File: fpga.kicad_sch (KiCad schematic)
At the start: 53 parts, among them Q1 BSS138PW, Q2 BSS138PW, Q3 BSS138PW, Q4 BSS138PW, SW1 SW_B3U-1000P_SMD, U1 ICE40UP5K-SG48, U2 FT232H_QFN, U3 W25Q32JW_SOIC-8

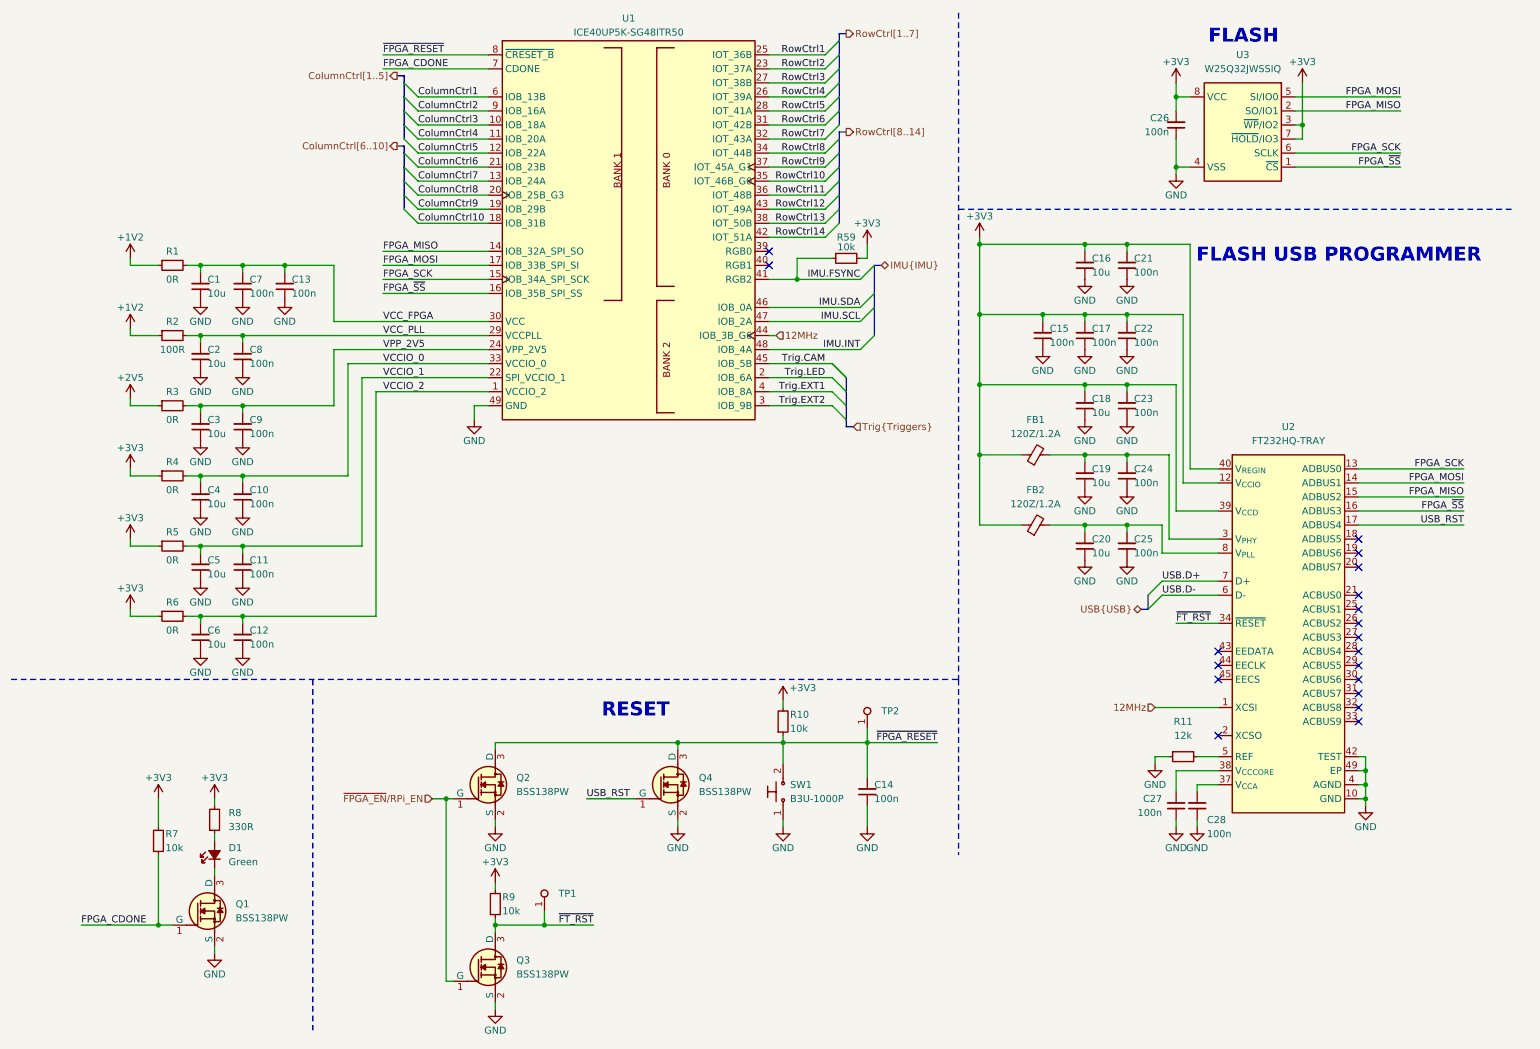
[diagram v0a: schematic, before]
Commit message: [#72133] Sch: Update control hierarchy
Signed-off-by: Dawid Lentka <dlentka@antmicro.com>
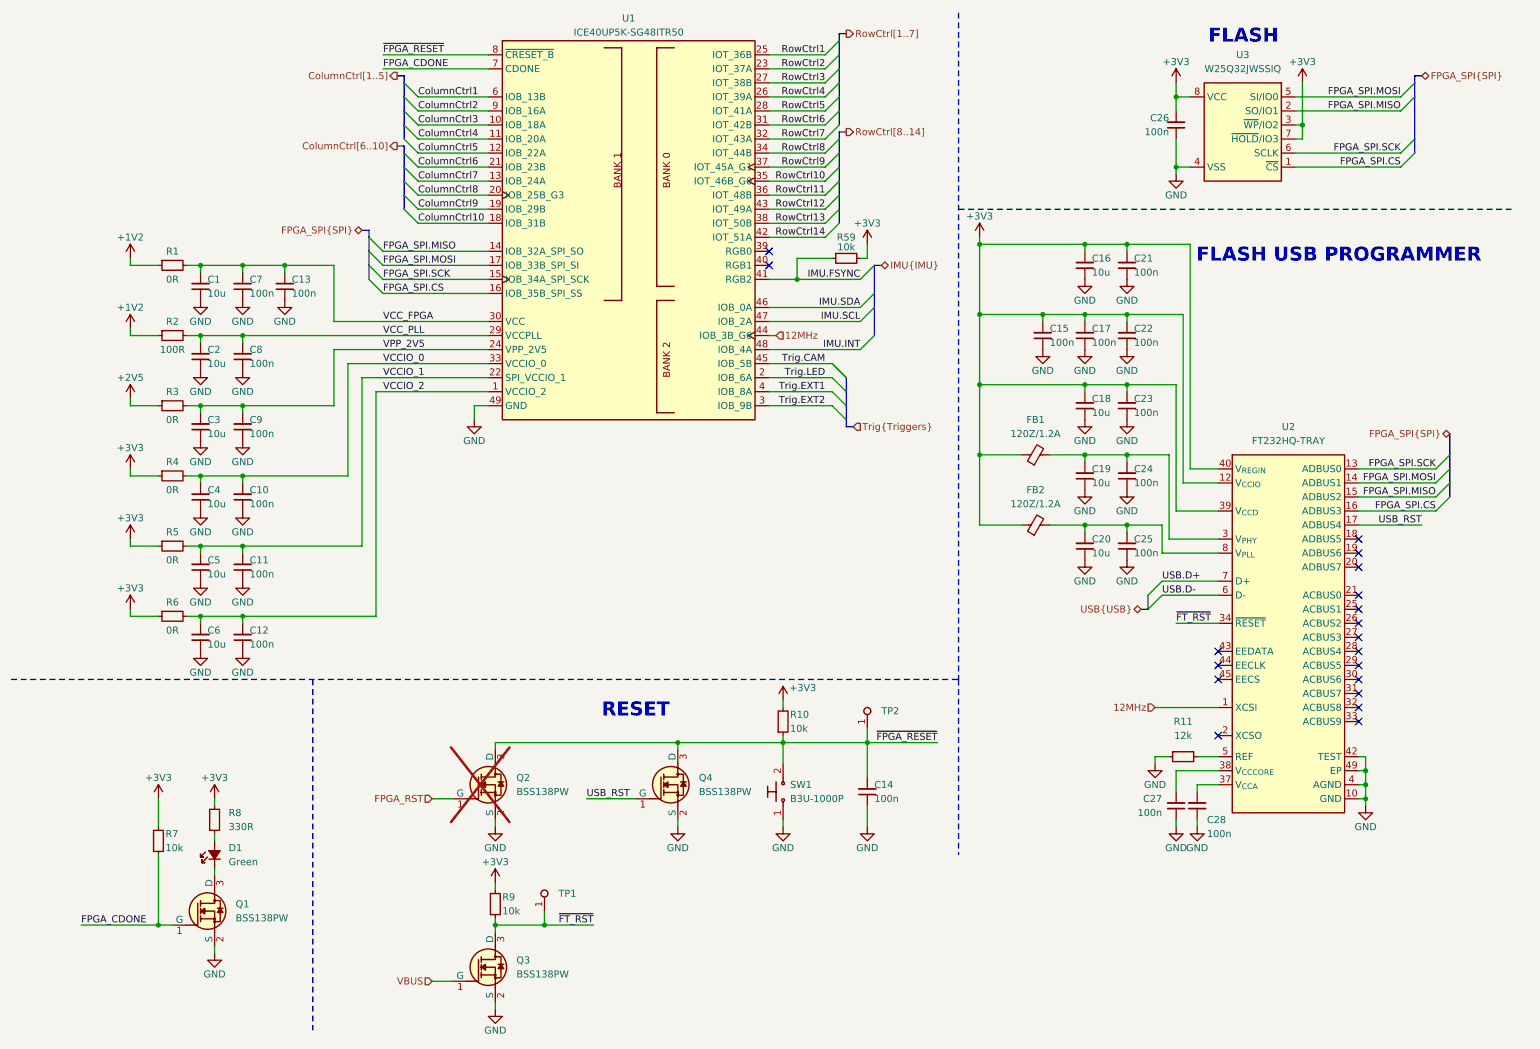
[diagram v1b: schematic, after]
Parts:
- Q2: now not fitted
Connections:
- net FPGA_MISO renamed FPGA_SPI.MISO
- net FPGA_MOSI renamed FPGA_SPI.MOSI
- net FPGA_SCK renamed FPGA_SPI.SCK
- net FPGA_~{SS} renamed FPGA_SPI.CS
- net ~{FPGA_EN}/RPi_EN renamed FPGA_RST
- net FPGA_RST: no longer Q3.1 (G)
- new net VBUS: Q3.1 (G)

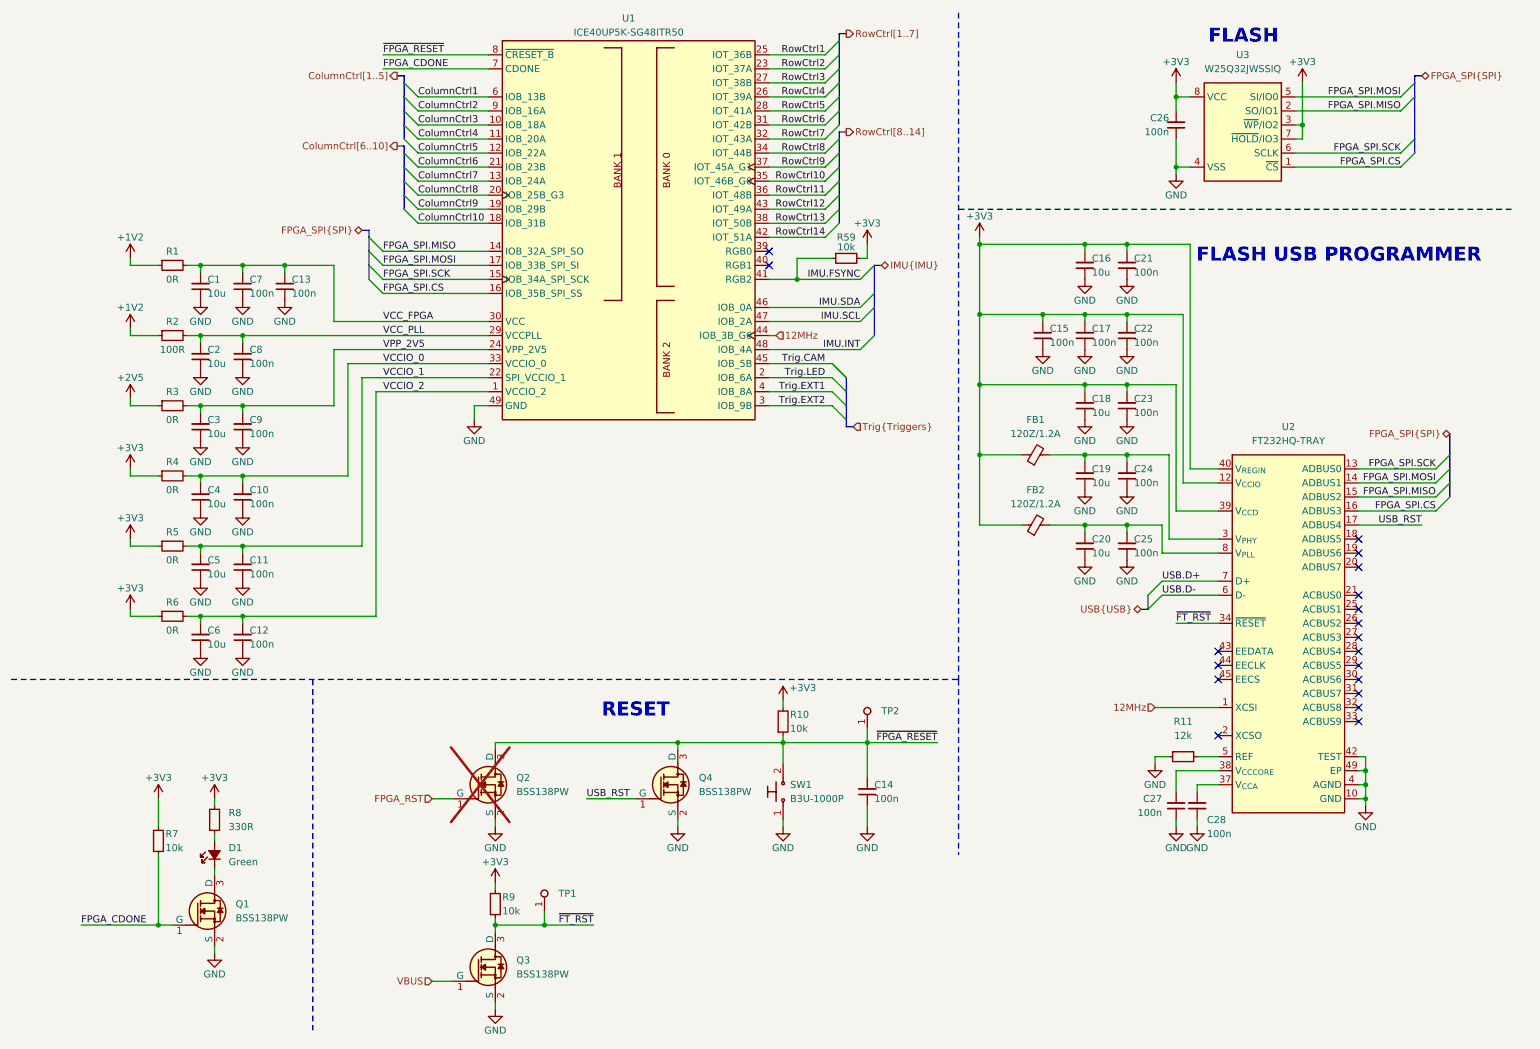
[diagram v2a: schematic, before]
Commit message: [#72133] Update USB FTDI sheet
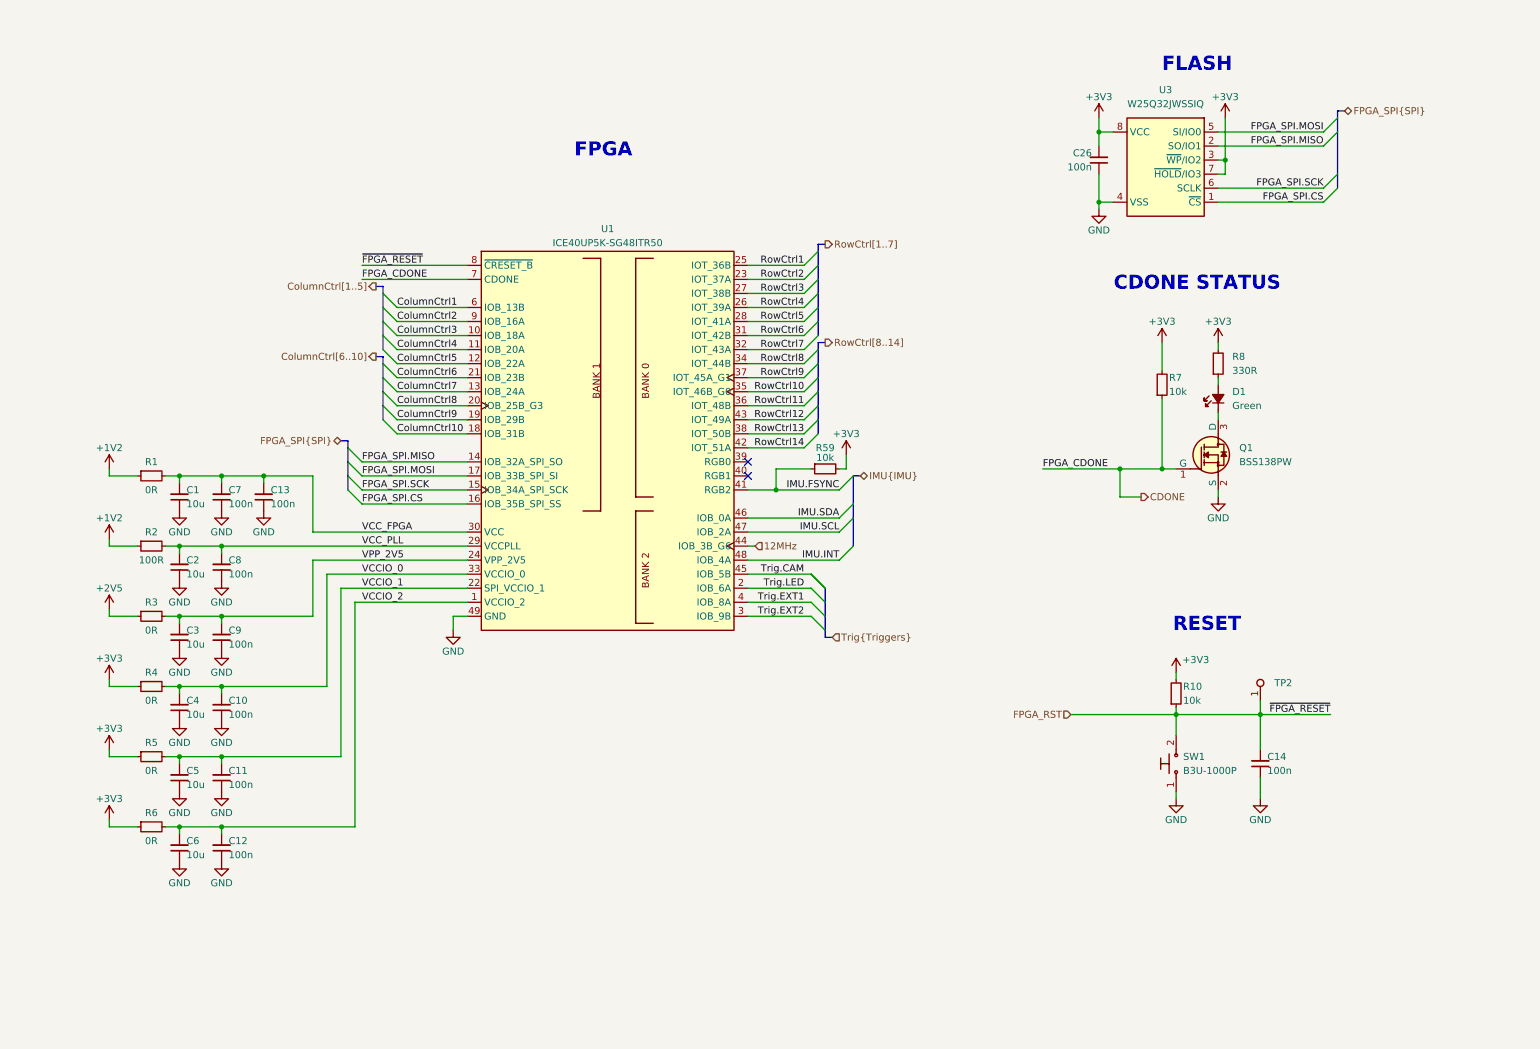
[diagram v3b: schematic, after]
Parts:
- removed C15, C17, C21, C22, C23, C24, C25, C27, C28: C_100n_0402, antmicro-footprints:C_0402_1005Metric, symbol antmicroCapacitors0402:C_100n_0402
- removed C16, C18, C19, C20: C_10u_10V_0402, antmicro-footprints:C_0402_1005Metric, symbol antmicroCapacitors0402:C_10u_10V_0402
- removed FB1, FB2: FB_120Z_1.2A_TDK-MPZ_0402, antmicro-footprints:FB_0402_1005Metric, symbol antmicroFerriteBeadsandChips:FB_120Z_1.2A_TDK-MPZ_0402
- removed Q2, Q3, Q4: BSS138PW, antmicro-footprints:SC70-3, symbol antmicroTransistorsFETsMOSFETsSingle:BSS138PW
- removed R11: R_12k_0402, antmicro-footprints:R_0402_1005Metric, symbol antmicroResistors0402:R_12k_0402
- removed R9: R_10k_0402, antmicro-footprints:R_0402_1005Metric, symbol antmicroResistors0402:R_10k_0402
- removed TP1: TP_0.75mm_SMD, antmicro-footprints:TP_SMD_0.75mm, symbol antmicroTestPoints:TP_0.75mm_SMD
- removed U2: FT232H_QFN, antmicro-footprints:QFN-48-1EP_8x8mm_P0.5mm_EP6.2x6.2mm_FT232HQ_marking, symbol antmicroInterfaceControllers:FT232H_QFN
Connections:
- net ~{FPGA_RESET} is gone; now on net FPGA_RST: C14.2, R10.1, SW1.2, TP2.1, U1.8 (~{CRESET_B})
- net FPGA_CDONE renamed CDONE
- no-connect marks 19 -> 2
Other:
- note added: "CDONE STATUS"
- note added: "FPGA"
- note removed: "FLASH USB PROGRAMMER"
- moved on the sheet: C1, C10, C11, C12, C13, C14, C2, C26, C3, C4, C5, C6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

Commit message: [#72133] Clean ERC
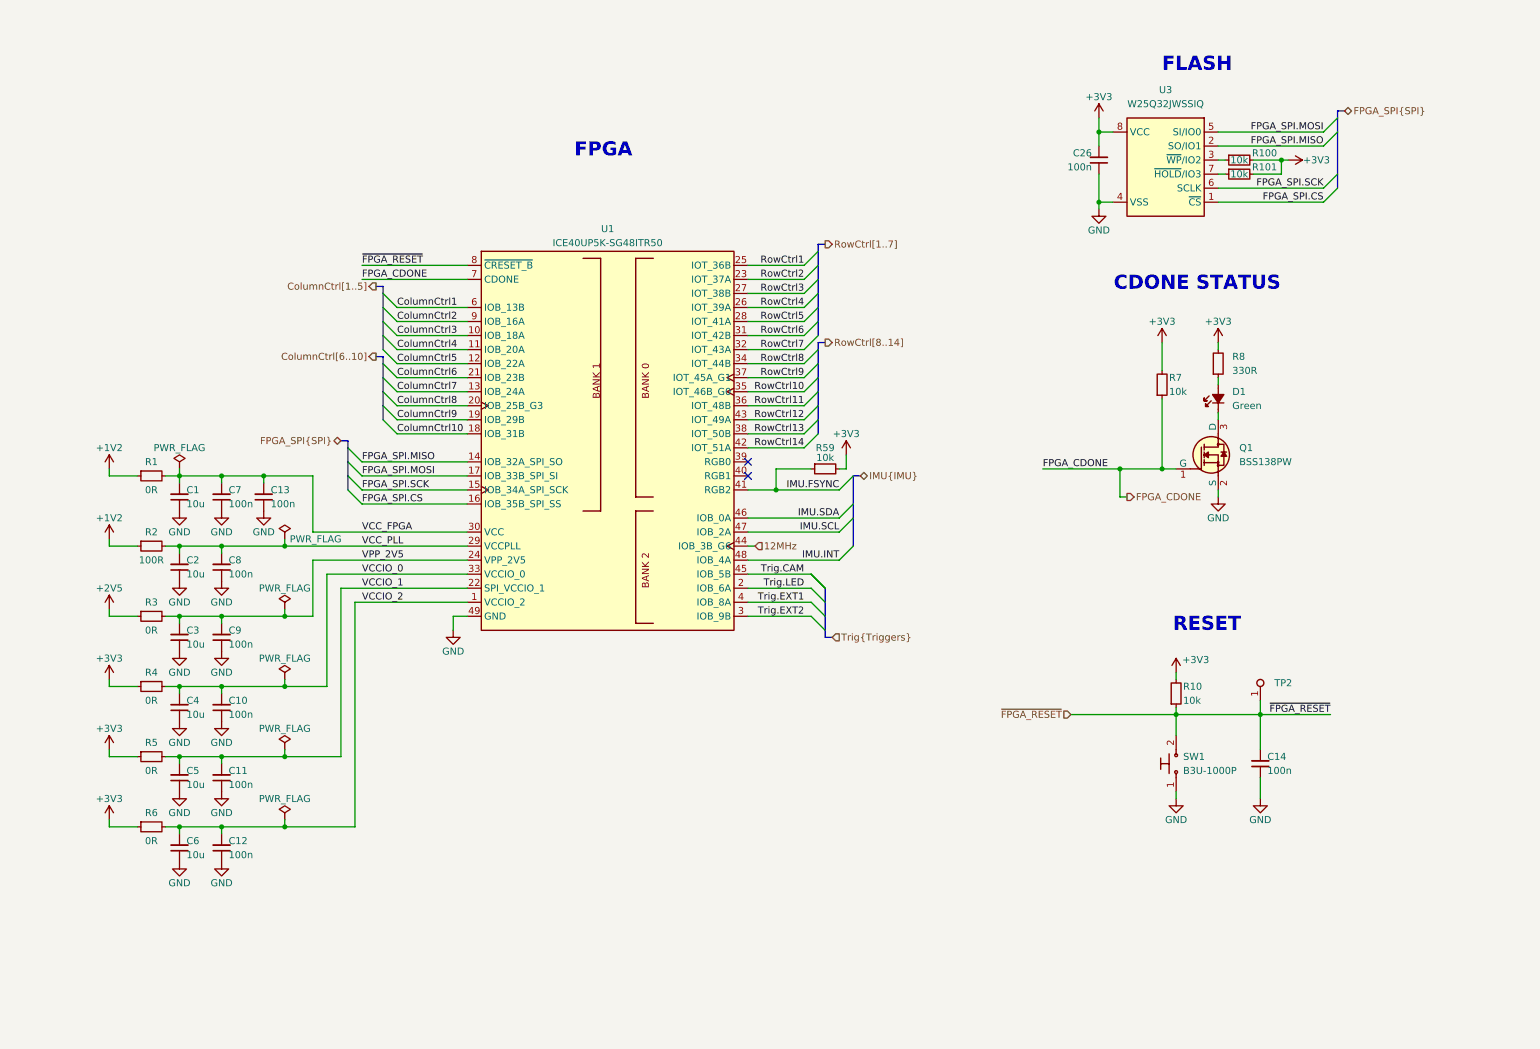
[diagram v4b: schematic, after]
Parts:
- added R100, R101: R_10k_0402, antmicro-footprints:R_0402_1005Metric, symbol antmicroResistors0402:R_10k_0402
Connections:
- net +3V3: now also R100.2, R101.2; no longer U3.3 (~{WP}/IO2), U3.7 (~{HOLD}/IO3)
- net CDONE renamed FPGA_CDONE
- net FPGA_RST renamed ~{FPGA_RESET}
- new net: R101.1, U3.7 (~{HOLD}/IO3)
- new net: R100.1, U3.3 (~{WP}/IO2)
